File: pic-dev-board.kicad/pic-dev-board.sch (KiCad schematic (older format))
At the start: 47 parts

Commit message: moved shift-register to hierarchical sheet / completed connections
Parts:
- removed D? (x8): LED, LED_THT:LED_D3.0mm, symbol Device:LED
- removed J? (x2): Conn_01x05, Connector_PinHeader_2.54mm:PinHeader_1x05_P2.54mm_Vertical, symbol Connector_Generic:Conn_01x05
- removed J?: Jumper, Connector_PinHeader_2.54mm:PinHeader_1x02_P2.54mm_Vertical, symbol Connector:Conn_01x02_Male
- removed J?: Conn_01x08_Male, Connector_PinHeader_2.54mm:PinHeader_1x08_P2.54mm_Vertical, symbol Connector:Conn_01x08_Male
- removed RN?: 680, Resistor_THT:R_Array_SIP9, symbol Device:R_Network08
- removed U?: 74HC595, Package_DIP:DIP-16_W7.62mm_Socket, symbol 74xx:74HC595
- added J7: Conn_TRISC, symbol Connector:Conn_01x08_Male
- added J9: Conn_TRISB, symbol Connector:Conn_01x04_Male
- J8: renamed from J?; value Conn_01x05_Male -> Conn_TRISA
- gave numbers to parts that had none: 32
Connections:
- net labels added: D4, D5, D6, D7, RB4, RB5, RB6, RB7, RC0, RC1, RC2, RC3, RC4, RC5, RC6, RC7, RS
- net labels removed: +5VP, CLK, DAT, QA, QB, QC, QD, QE, QF, QG, QH, ~MCLR
- wire segments 126 -> 62
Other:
- note added: "TRISB"
- note added: "TRISC"
- note removed: "Vin\nSERin\nSCLKin\nRCLKin\nGND"
- note removed: "Vout\nSERout\nSCLKout\nRCLKout\nGND"
- moved on the sheet: D6, J6, R11, R12, R13, R14, SW1

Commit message: added power-connector (barrel-jack)
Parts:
- added J15: Barrel_Jack_Switch, symbol Connector:Barrel_Jack_Switch
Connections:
- net +5V: now also J15.1
- net GND: now also J15.2
- no-connect marks 5 -> 6
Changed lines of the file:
@@
 Sheet 1 2
 Title "PIC Development Board"
-Date "2020-08-11"
+Date "2020-08-13"
 Rev "1"
 Comp "Bernhard Bablok"
-Comment1 "https://github.com/bablokb/pcb-pic12-dev"
+Comment1 "https://github.com/bablokb/pcb-pic-devboard"
 Comment2 ""
 Comment3 ""
@@
 Text Label 1950 4750 0    50   ~ 0
 Vdd
-Wire Wire Line
-	5200 5650 5200 5750
 $Comp
 L Device:LED D1
@@
 	-1   0    0    -1
 $EndComp
-Wire Wire Line
-	5200 4050 5200 3950
 Connection ~ 5200 4050
 Connection ~ 4800 4050
@@
 L power:PWR_FLAG #FLG0101
 U 1 1 5F3F0293
-P 5200 5750
-F 0 "#FLG0101" H 5200 5825 50  0001 C CNN
-F 1 "PWR_FLAG" V 5200 5878 50  0000 L CNN
-F 2 "" H 5200 5750 50  0001 C CNN
-F 3 "~" H 5200 5750 50  0001 C CNN
-	1    5200 5750
+P 5400 6950
+F 0 "#FLG0101" H 5400 7025 50  0001 C CNN
+F 1 "PWR_FLAG" V 5400 7078 50  0000 L CNN
+F 2 "" H 5400 6950 50  0001 C CNN
+F 3 "~" H 5400 6950 50  0001 C CNN
+	1    5400 6950
 	0    1    1    0
 $EndComp
-Connection ~ 5200 5750
-Wire Wire Line
-	5200 5750 5200 5850
 $Comp
 L power:PWR_FLAG #FLG0102
 U 1 1 5F3F0E86
-P 5600 3850
-F 0 "#FLG0102" H 5600 3925 50  0001 C CNN
-F 1 "PWR_FLAG" H 5600 4023 50  0000 C CNN
-F 2 "" H 5600 3850 50  0001 C CNN
-F 3 "~" H 5600 3850 50  0001 C CNN
-	1    5600 3850
-	1    0    0    -1
-$EndComp
-Wire Wire Line
-	5600 3850 5600 3950
-Wire Wire Line
-	5600 3950 5200 3950
-Connection ~ 5200 3950
-Wire Wire Line
-	5200 3950 5200 3900
+P 5450 6700
+F 0 "#FLG0102" H 5450 6775 50  0001 C CNN
+F 1 "PWR_FLAG" H 5450 6873 50  0000 C CNN
+F 2 "" H 5450 6700 50  0001 C CNN
+F 3 "~" H 5450 6700 50  0001 C CNN
+	1    5450 6700
+	1    0    0    -1
+$EndComp
 Wire Wire Line
 	8550 4450 8550 5200
@@
 Wire Wire Line
 	9350 5200 8850 5200
+$Comp
+L Connector:Barrel_Jack_Switch J15
+U 1 1 5F353FBE
+P 4600 6850
+F 0 "J15" H 4657 7167 50  0000 C CNN
+F 1 "Barrel_Jack_Switch" H 4657 7076 50  0000 C CNN
+F 2 "" H 4650 6810 50  0001 C CNN
+F 3 "~" H 4650 6810 50  0001 C CNN
+	1    4600 6850
+	1    0    0    -1
+$EndComp
+NoConn ~ 4900 6850
+$Comp
+L power:GND #PWR0103
+U 1 1 5F362EB6
+P 5150 7150
+F 0 "#PWR0103" H 5150 6900 50  0001 C CNN
+F 1 "GND" H 5155 6977 50  0000 C CNN
+F 2 "" H 5150 7150 50  0001 C CNN
+F 3 "" H 5150 7150 50  0001 C CNN
+	1    5150 7150
+	1    0    0    -1
+$EndComp
+$Comp
+L power:+5V #PWR0104
+U 1 1 5F363A77
+P 5150 6600
+F 0 "#PWR0104" H 5150 6450 50  0001 C CNN
+F 1 "+5V" H 5165 6773 50  0000 C CNN
+F 2 "" H 5150 6600 50  0001 C CNN
+F 3 "" H 5150 6600 50  0001 C CNN
+	1    5150 6600
+	1    0    0    -1
+$EndComp
+Wire Wire Line
+	4900 6750 5150 6750
+Wire Wire Line
+	5150 6750 5150 6600
+Wire Wire Line
+	4900 6950 5150 6950
+Wire Wire Line
+	5150 6950 5150 7150
+Wire Wire Line
+	5150 6750 5450 6750
+Wire Wire Line
+	5450 6750 5450 6700
+Connection ~ 5150 6750
+Wire Wire Line
+	5200 5650 5200 5850
+Wire Wire Line
+	5150 6950 5400 6950
+Connection ~ 5150 6950
+Wire Wire Line
+	5200 3900 5200 4050
 $EndSCHEMATC

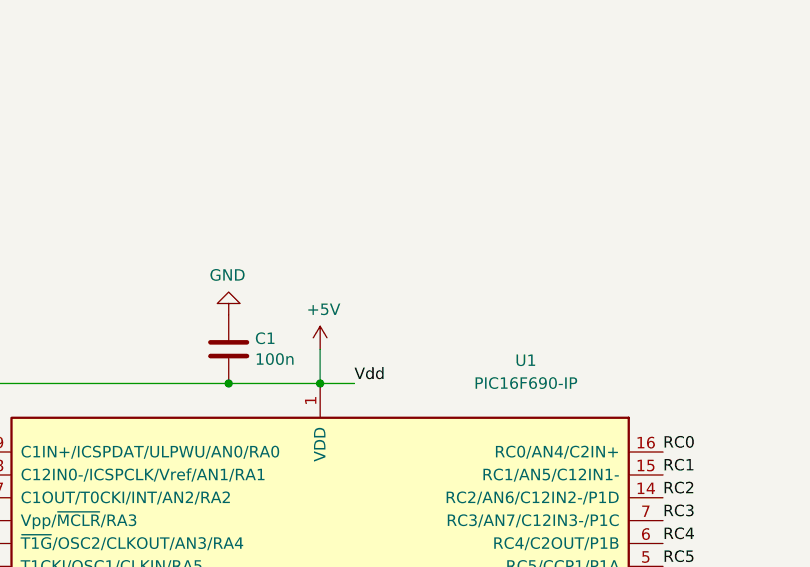
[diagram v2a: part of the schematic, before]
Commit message: added jumper to isolate +5V during programming
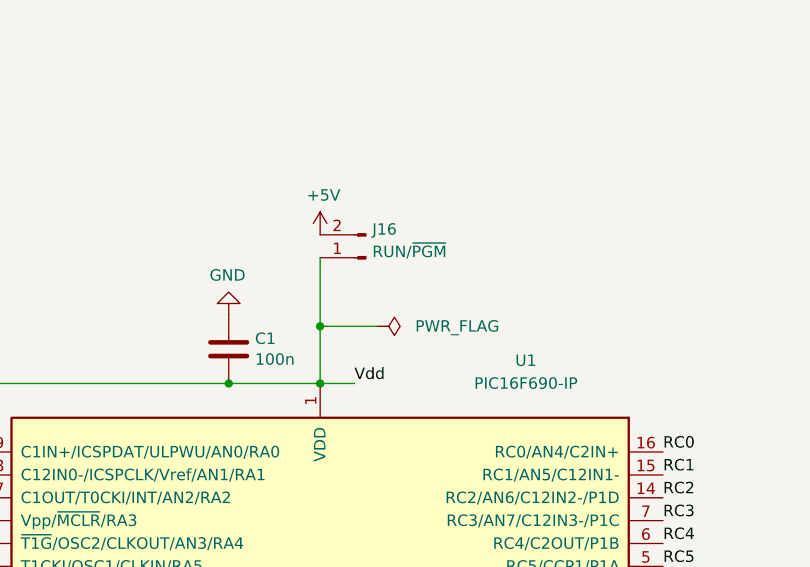
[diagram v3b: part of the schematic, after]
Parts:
- added J16: RUN/~PGM, symbol Connector:Conn_01x02_Male
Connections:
- net +5V: now also J16.2 (Pin_2); no longer C1.2, D6.2 (A), J6.2 (Pin_2), U1.1 (VDD)
- new net Vdd: C1.2, D6.2 (A), J16.1 (Pin_1), J6.2 (Pin_2), U1.1 (VDD)
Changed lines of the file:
@@
 L power:+5V #PWR013
 U 1 1 5F36CAAF
-P 5200 3900
-F 0 "#PWR013" H 5200 3750 50  0001 C CNN
-F 1 "+5V" H 5215 4073 50  0000 C CNN
-F 2 "" H 5200 3900 50  0001 C CNN
-F 3 "" H 5200 3900 50  0001 C CNN
-	1    5200 3900
+P 5200 3400
+F 0 "#PWR013" H 5200 3250 50  0001 C CNN
+F 1 "+5V" H 5215 3573 50  0000 C CNN
+F 2 "" H 5200 3400 50  0001 C CNN
+F 3 "" H 5200 3400 50  0001 C CNN
+	1    5200 3400
 	1    0    0    -1
 $EndComp
@@
 	5150 6950 5400 6950
 Connection ~ 5150 6950
-Wire Wire Line
-	5200 3900 5200 4050
+$Comp
+L Connector:Conn_01x02_Male J16
+U 1 1 5F36E374
+P 5400 3500
+F 0 "J16" H 5372 3376 50  0000 R CNN
+F 1 "RUN/~PGM" H 5372 3474 50  0000 R CNN
+F 2 "" H 5400 3500 50  0001 C CNN
+F 3 "~" H 5400 3500 50  0001 C CNN
+	1    5400 3500
+	-1   0    0    1
+$EndComp
+Wire Wire Line
+	5200 3500 5200 3800
+$Comp
+L power:PWR_FLAG #FLG0104
+U 1 1 5F37108D
+P 5450 3800
+F 0 "#FLG0104" H 5450 3875 50  0001 C CNN
+F 1 "PWR_FLAG" V 5450 4150 50  0000 C CNN
+F 2 "" H 5450 3800 50  0001 C CNN
+F 3 "~" H 5450 3800 50  0001 C CNN
+	1    5450 3800
+	0    1    1    0
+$EndComp
+Connection ~ 5200 3800
+Wire Wire Line
+	5200 3800 5200 4050
+Wire Wire Line
+	5200 3800 5450 3800
 $EndSCHEMATC

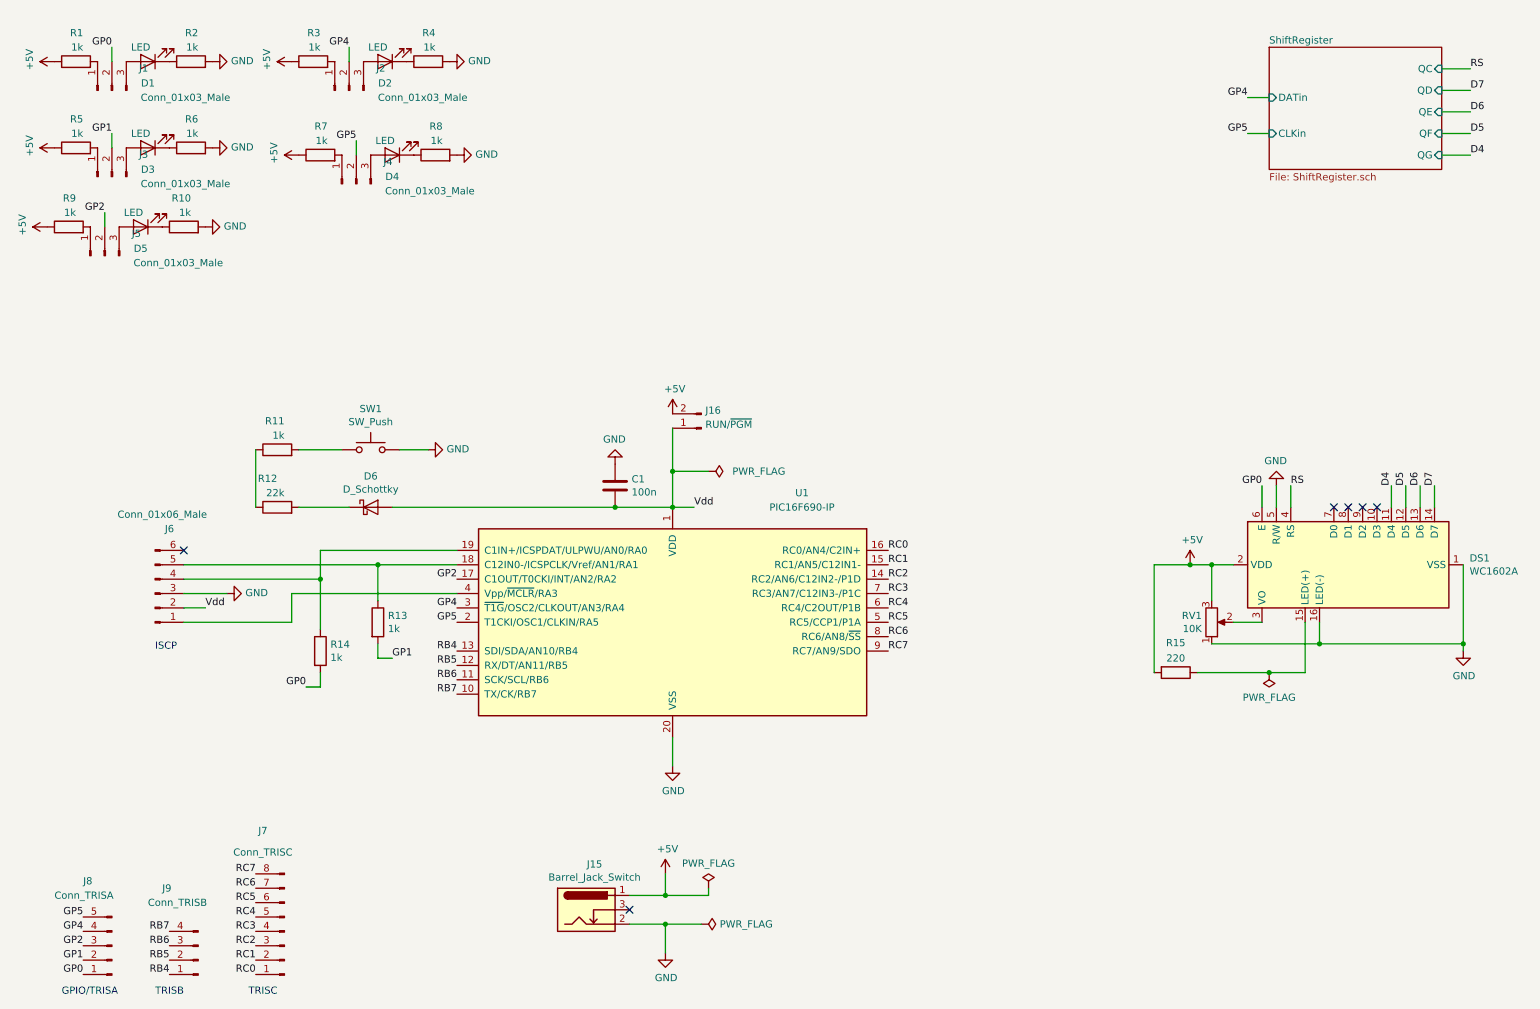
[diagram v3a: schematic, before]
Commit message: added I2C-connector
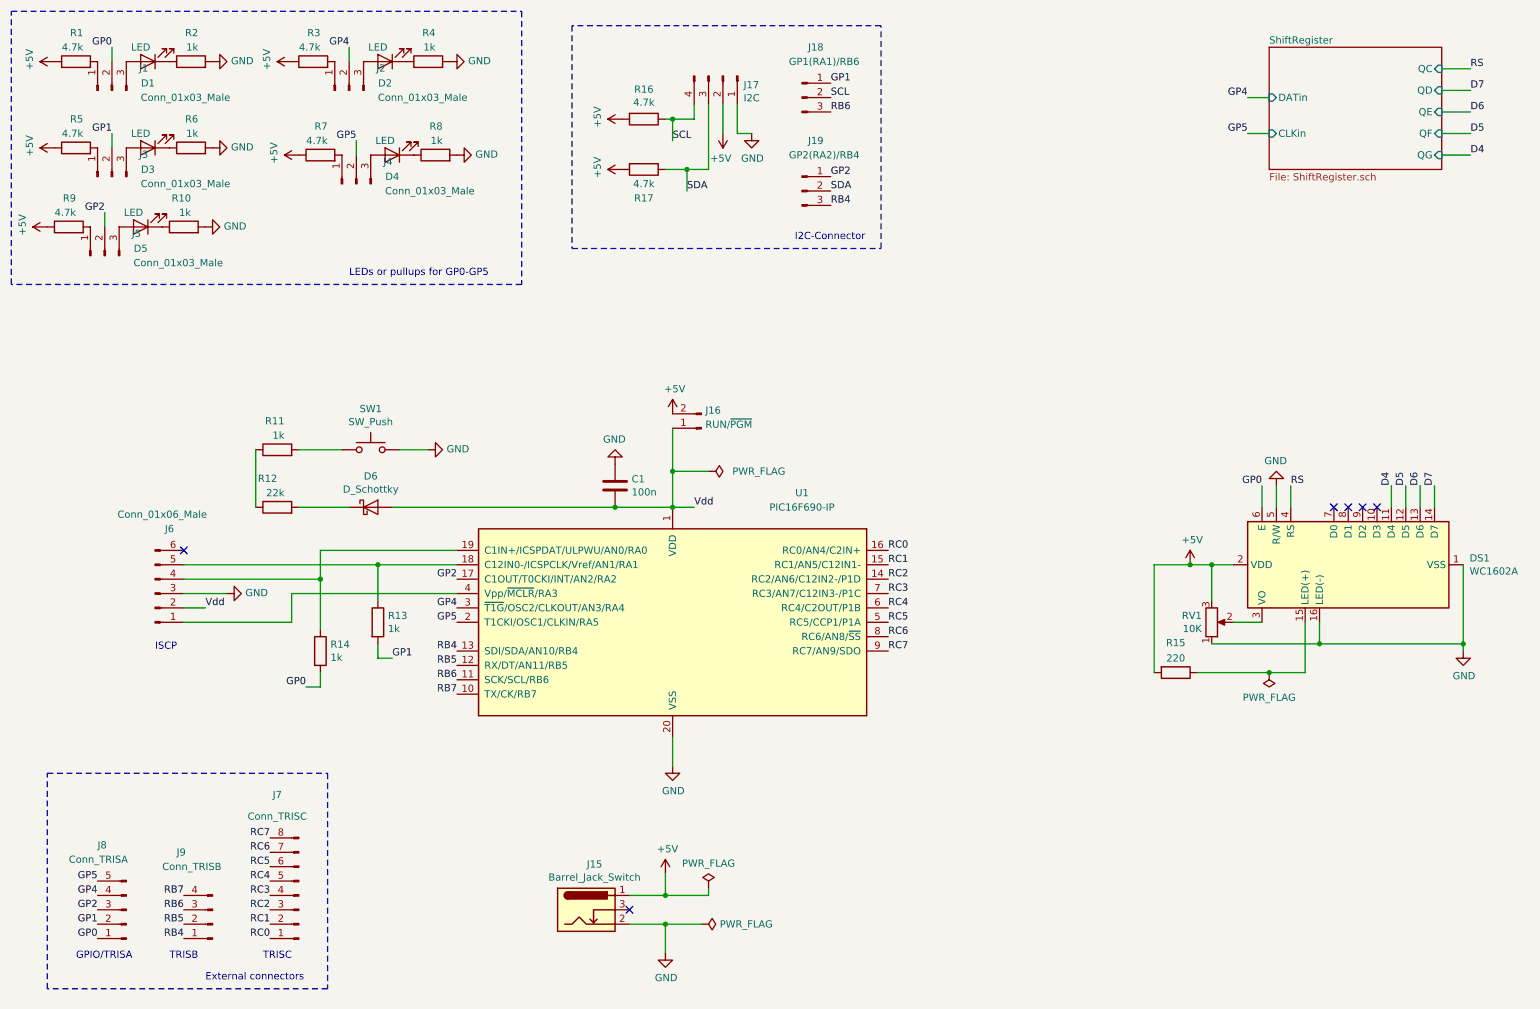
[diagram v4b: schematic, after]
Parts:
- added J17: I2C, symbol Connector:Conn_01x04_Male
- added J18: GP1(RA1)/RB6, symbol Connector:Conn_01x03_Male
- added J19: GP2(RA2)/RB4, symbol Connector:Conn_01x03_Male
- added R16, R17: 4.7k, symbol Device:R
- R1, R3, R5, R7, R9: value 1k -> 4.7k
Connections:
- net +5V: now also J17.2 (Pin_2), R16.2, R17.2
- net GND: now also J17.1 (Pin_1)
- net GP1: now also J18.1 (Pin_1)
- net GP2: now also J19.1 (Pin_1)
- net RB4: now also J19.3 (Pin_3)
- net RB6: now also J18.3 (Pin_3)
- new net SCL: J17.4 (Pin_4), J18.2 (Pin_2), R16.1
- new net SDA: J17.3 (Pin_3), J19.2 (Pin_2), R17.1
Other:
- note added: "External connectors"
- note added: "I2C-Connector"
- note added: "LEDs or pullups for GP0-GP5"
- moved on the sheet: J7, J8, J9
